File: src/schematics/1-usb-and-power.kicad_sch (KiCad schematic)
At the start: 49 parts, among them Q101 NX6008NBKW, U101 MP5016HGQH, U102 BQ24392RSER, U103 FUSB302BMPX, U104 TPS628512DRLR

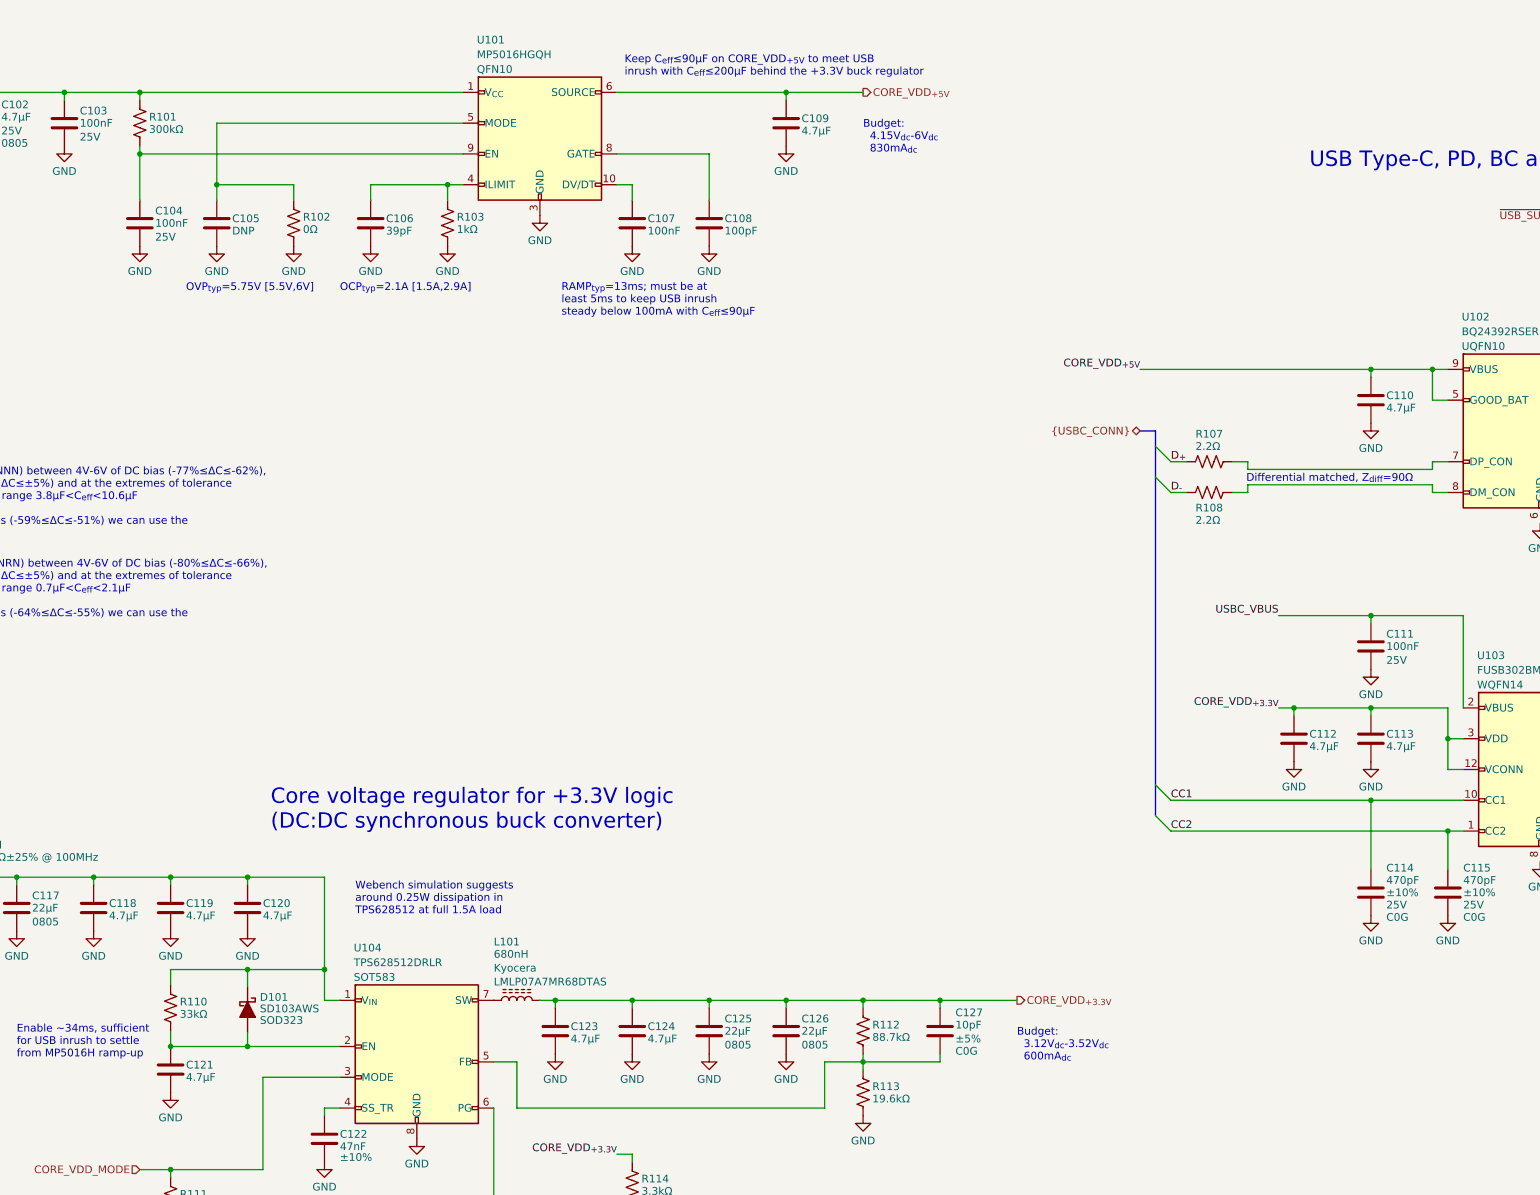
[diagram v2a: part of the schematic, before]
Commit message: Finished drawing up the audio output schematic.  The speaker selection is still to do.
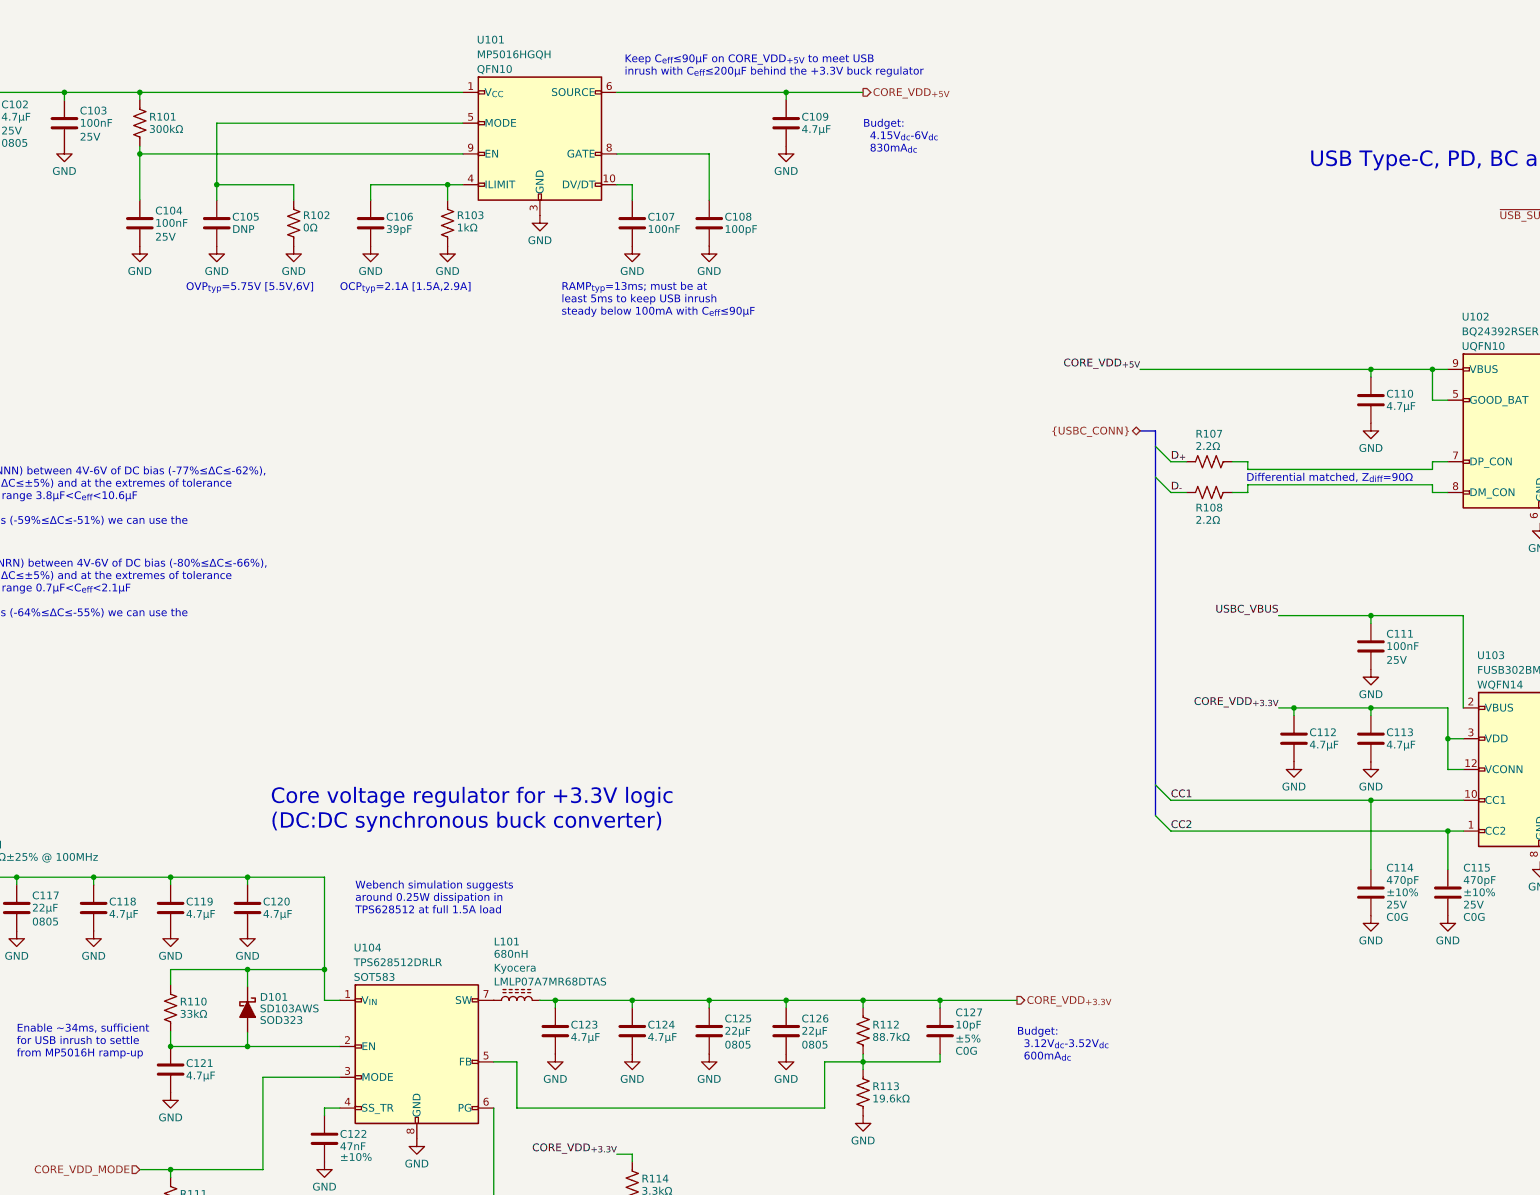
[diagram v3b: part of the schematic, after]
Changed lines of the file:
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@@
   (symbol (lib_id "restall-generic-capacitors:capacitor-unpolarised") (at 167.64 85.09 0) (unit 1)
     (in_bom yes) (on_board yes) (dnp no)
-    (property "Reference" "C108" (at 170.18 84.328 0)
+    (property "Reference" "C108" (at 170.18 84.074 0)
       (effects (font (size 1.27 1.27)) (justify left))
     )
-    (property "Value" "100pF" (at 170.18 86.36 0)
+    (property "Value" "100pF" (at 170.18 86.106 0)
       (effects (font (size 1.27 1.27)) (justify left))
     )
@@
   (symbol (lib_id "restall-generic-capacitors:capacitor-unpolarised") (at 142.24 218.44 0) (unit 1)
     (in_bom yes) (on_board yes) (dnp no)
-    (property "Reference" "C123" (at 144.78 217.678 0)
+    (property "Reference" "C123" (at 144.78 217.424 0)
       (effects (font (size 1.27 1.27)) (justify left))
     )
-    (property "Value" "4.7μF" (at 144.78 219.71 0)
+    (property "Value" "4.7μF" (at 144.78 219.456 0)
       (effects (font (size 1.27 1.27)) (justify left))
     )
@@
   (symbol (lib_id "restall-generic-resistors:resistor") (at 124.46 85.09 0) (unit 1)
     (in_bom yes) (on_board yes) (dnp no)
-    (property "Reference" "R103" (at 125.984 84.074 0)
+    (property "Reference" "R103" (at 125.984 83.82 0)
       (effects (font (size 1.27 1.27)) (justify left))
     )
-    (property "Value" "1kΩ" (at 125.984 86.106 0)
+    (property "Value" "1kΩ" (at 125.984 85.852 0)
       (effects (font (size 1.27 1.27)) (justify left))
     )
@@
   (symbol (lib_id "restall-generic-capacitors:capacitor-unpolarised") (at 66.04 198.12 0) (unit 1)
     (in_bom yes) (on_board yes) (dnp no)
-    (property "Reference" "C118" (at 68.58 197.358 0)
+    (property "Reference" "C118" (at 68.58 197.104 0)
       (effects (font (size 1.27 1.27)) (justify left))
     )
-    (property "Value" "4.7μF" (at 68.58 199.39 0)
+    (property "Value" "4.7μF" (at 68.58 199.136 0)
       (effects (font (size 1.27 1.27)) (justify left))
     )
@@
   (symbol (lib_id "restall-generic-capacitors:capacitor-unpolarised") (at 264.16 170.18 0) (unit 1)
     (in_bom yes) (on_board yes) (dnp no)
-    (property "Reference" "C112" (at 266.7 169.418 0)
+    (property "Reference" "C112" (at 266.7 169.164 0)
       (effects (font (size 1.27 1.27)) (justify left))
     )
-    (property "Value" "4.7μF" (at 266.7 171.45 0)
+    (property "Value" "4.7μF" (at 266.7 171.196 0)
       (effects (font (size 1.27 1.27)) (justify left))
     )
@@
   (symbol (lib_id "restall-generic-capacitors:capacitor-unpolarised") (at 276.86 170.18 0) (unit 1)
     (in_bom yes) (on_board yes) (dnp no)
-    (property "Reference" "C113" (at 279.4 169.418 0)
+    (property "Reference" "C113" (at 279.4 169.164 0)
       (effects (font (size 1.27 1.27)) (justify left))
     )
-    (property "Value" "4.7μF" (at 279.4 171.45 0)
+    (property "Value" "4.7μF" (at 279.4 171.196 0)
       (effects (font (size 1.27 1.27)) (justify left))
     )
@@
   (symbol (lib_id "restall-generic-capacitors:capacitor-unpolarised") (at 154.94 218.44 0) (unit 1)
     (in_bom yes) (on_board yes) (dnp no)
-    (property "Reference" "C124" (at 157.48 217.678 0)
+    (property "Reference" "C124" (at 157.48 217.424 0)
       (effects (font (size 1.27 1.27)) (justify left))
     )
-    (property "Value" "4.7μF" (at 157.48 219.71 0)
+    (property "Value" "4.7μF" (at 157.48 219.456 0)
       (effects (font (size 1.27 1.27)) (justify left))
     )
@@
   (symbol (lib_id "restall-generic-capacitors:capacitor-unpolarised") (at 78.74 224.79 0) (unit 1)
     (in_bom yes) (on_board yes) (dnp no)
-    (property "Reference" "C121" (at 81.28 224.028 0)
+    (property "Reference" "C121" (at 81.28 223.774 0)
       (effects (font (size 1.27 1.27)) (justify left))
     )
-    (property "Value" "4.7μF" (at 81.28 226.06 0)
+    (property "Value" "4.7μF" (at 81.28 225.806 0)
       (effects (font (size 1.27 1.27)) (justify left))
     )
@@
   (symbol (lib_id "restall-generic-capacitors:capacitor-unpolarised") (at 180.34 68.58 0) (unit 1)
     (in_bom yes) (on_board yes) (dnp no)
-    (property "Reference" "C109" (at 182.88 67.818 0)
+    (property "Reference" "C109" (at 182.88 67.564 0)
       (effects (font (size 1.27 1.27)) (justify left))
     )
-    (property "Value" "4.7μF" (at 182.88 69.85 0)
+    (property "Value" "4.7μF" (at 182.88 69.596 0)
       (effects (font (size 1.27 1.27)) (justify left))
     )
@@
   (symbol (lib_id "restall-generic-capacitors:capacitor-unpolarised") (at 276.86 114.3 0) (unit 1)
     (in_bom yes) (on_board yes) (dnp no)
-    (property "Reference" "C110" (at 279.4 113.538 0)
+    (property "Reference" "C110" (at 279.4 113.284 0)
       (effects (font (size 1.27 1.27)) (justify left))
     )
-    (property "Value" "4.7μF" (at 279.4 115.57 0)
+    (property "Value" "4.7μF" (at 279.4 115.316 0)
       (effects (font (size 1.27 1.27)) (justify left))
     )
@@
   (symbol (lib_id "restall-generic-capacitors:capacitor-unpolarised") (at 86.36 85.09 0) (unit 1)
     (in_bom no) (on_board yes) (dnp no)
-    (property "Reference" "C105" (at 88.9 84.328 0)
+    (property "Reference" "C105" (at 88.9 84.074 0)
       (effects (font (size 1.27 1.27)) (justify left))
     )
-    (property "Value" "DNP" (at 88.9 86.36 0)
+    (property "Value" "DNP" (at 88.9 86.106 0)
       (effects (font (size 1.27 1.27)) (justify left))
     )
@@
   (symbol (lib_id "restall-generic-resistors:resistor") (at 99.06 85.09 0) (unit 1)
     (in_bom yes) (on_board yes) (dnp no)
-    (property "Reference" "R102" (at 100.584 84.074 0)
+    (property "Reference" "R102" (at 100.584 83.82 0)
       (effects (font (size 1.27 1.27)) (justify left))
     )
-    (property "Value" "0Ω" (at 100.584 86.106 0)
+    (property "Value" "0Ω" (at 100.584 85.852 0)
       (effects (font (size 1.27 1.27)) (justify left))
     )
@@
   (symbol (lib_id "restall-generic-capacitors:capacitor-unpolarised") (at 111.76 85.09 0) (unit 1)
     (in_bom yes) (on_board yes) (dnp no)
-    (property "Reference" "C106" (at 114.3 84.328 0)
+    (property "Reference" "C106" (at 114.3 84.074 0)
       (effects (font (size 1.27 1.27)) (justify left))
     )
-    (property "Value" "39pF" (at 114.3 86.36 0)
+    (property "Value" "39pF" (at 114.3 86.106 0)
       (effects (font (size 1.27 1.27)) (justify left))
     )
@@
   (symbol (lib_id "restall-generic-capacitors:capacitor-unpolarised") (at 91.44 198.12 0) (unit 1)
     (in_bom yes) (on_board yes) (dnp no)
-    (property "Reference" "C120" (at 93.98 197.358 0)
+    (property "Reference" "C120" (at 93.98 197.104 0)
       (effects (font (size 1.27 1.27)) (justify left))
     )
-    (property "Value" "4.7μF" (at 93.98 199.39 0)
+    (property "Value" "4.7μF" (at 93.98 199.136 0)
       (effects (font (size 1.27 1.27)) (justify left))
     )
@@
   (symbol (lib_id "restall-generic-capacitors:capacitor-unpolarised") (at 78.74 198.12 0) (unit 1)
     (in_bom yes) (on_board yes) (dnp no)
-    (property "Reference" "C119" (at 81.28 197.358 0)
+    (property "Reference" "C119" (at 81.28 197.104 0)
       (effects (font (size 1.27 1.27)) (justify left))
     )
-    (property "Value" "4.7μF" (at 81.28 199.39 0)
+    (property "Value" "4.7μF" (at 81.28 199.136 0)
       (effects (font (size 1.27 1.27)) (justify left))
     )
@@
   (symbol (lib_id "restall-generic-capacitors:capacitor-unpolarised") (at 154.94 85.09 0) (unit 1)
     (in_bom yes) (on_board yes) (dnp no)
-    (property "Reference" "C107" (at 157.48 84.328 0)
+    (property "Reference" "C107" (at 157.48 84.074 0)
       (effects (font (size 1.27 1.27)) (justify left))
     )
-    (property "Value" "100nF" (at 157.48 86.36 0)
+    (property "Value" "100nF" (at 157.48 86.106 0)
       (effects (font (size 1.27 1.27)) (justify left))
     )
